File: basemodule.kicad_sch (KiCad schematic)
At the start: 6 parts, among them J1 Conn_01x05_Pin, J2 USB_C_Receptacle_USB2.0_14P, U1 ESP32-S3-WROOM-1, U2 LD1117S33TR_SOT223

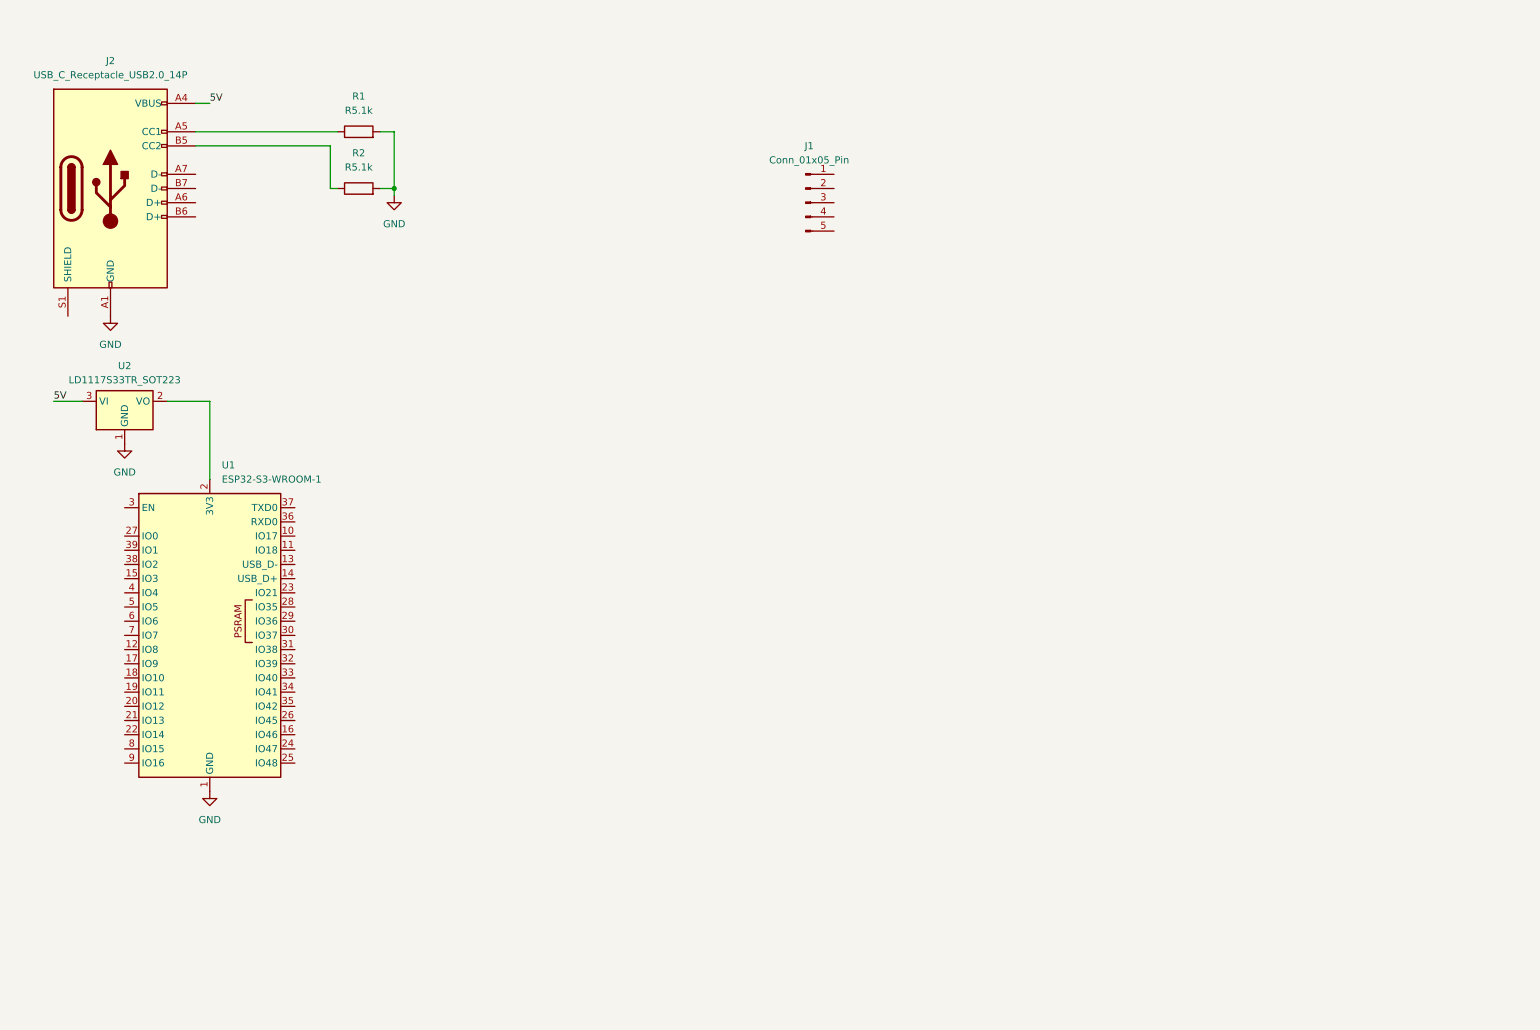
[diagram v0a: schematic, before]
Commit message: Added power components to base module schematic Higher-voltage (15V) USB PD is not complete, still need to read the datasheet for the PD chip. Also I just realized that PD chip is QFN, I have no idea how we are going to solder these onto the board. I hope we have access to a hot-air station or some other way of solder reflow.
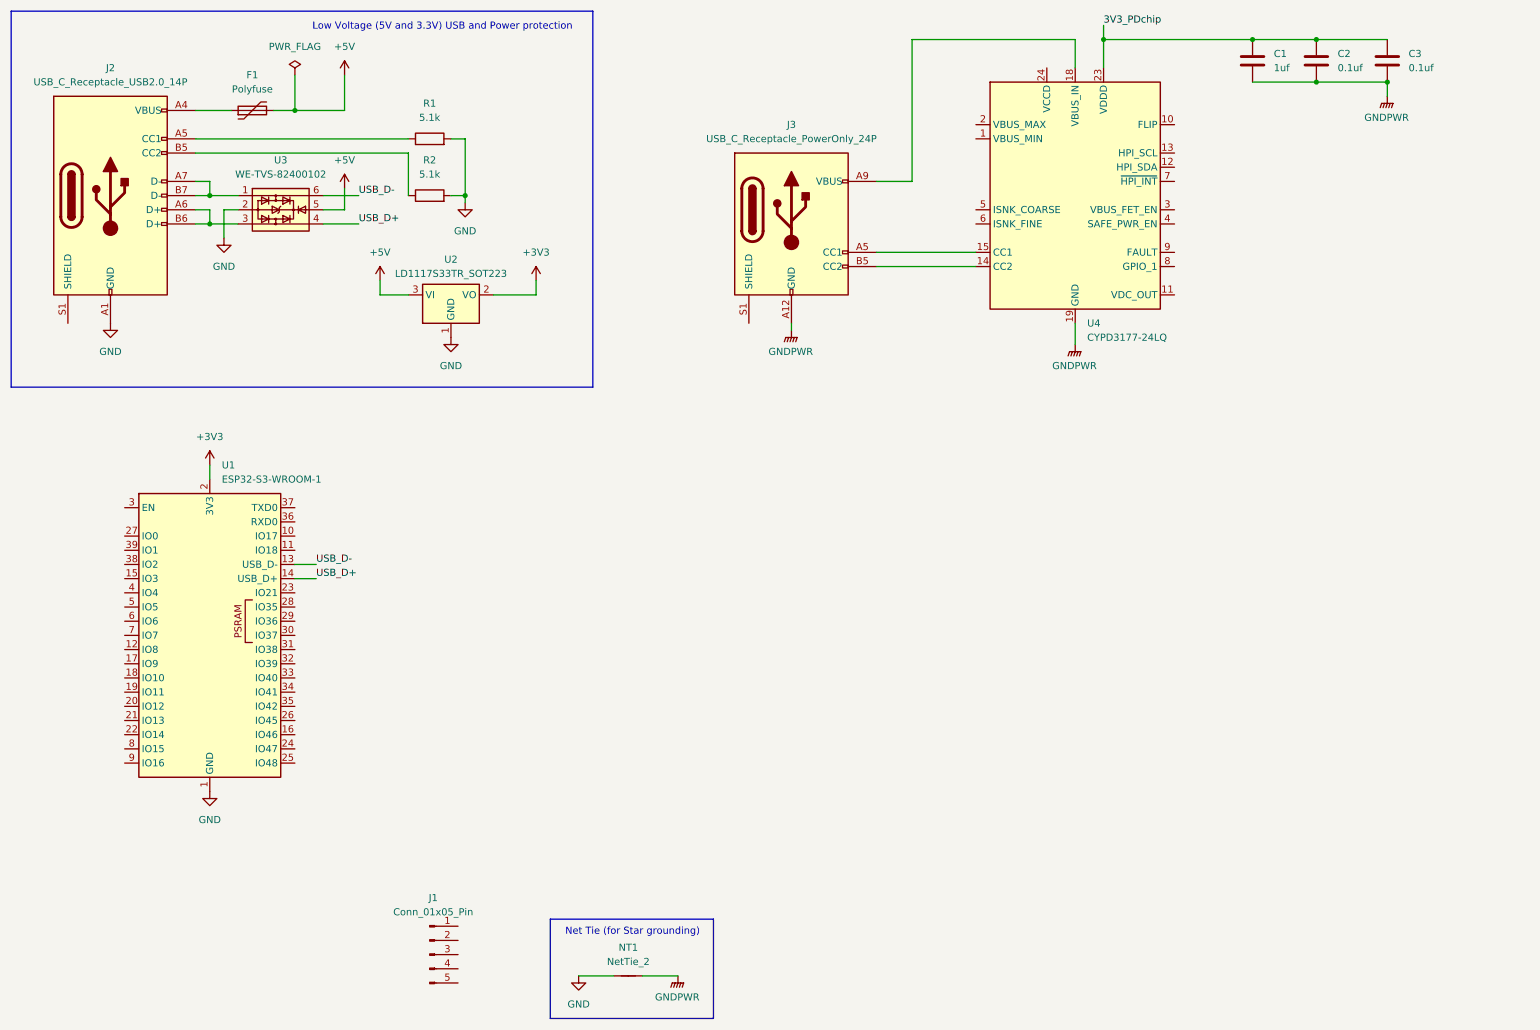
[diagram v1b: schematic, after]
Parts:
- added C1: 1uf, symbol Device:C
- added C2, C3: 0.1uf, symbol Device:C
- added F1: Polyfuse, Resistor_SMD:R_1206_3216Metric, symbol Device:Polyfuse
- added J3: USB_C_Receptacle_PowerOnly_24P, symbol Connector:USB_C_Receptacle_PowerOnly_24P
- added NT1: NetTie_2, symbol Device:NetTie_2
- added U3: WE-TVS-82400102, Package_TO_SOT_SMD:SOT-23-6, symbol Power_Protection:WE-TVS-82400102
- added U4: CYPD3177-24LQ, Package_DFN_QFN:QFN-24-1EP_4x4mm_P0.5mm_EP2.75x2.75mm, symbol Interface_USB:CYPD3177-24LQ
- R1, R2: value R5.1k -> 5.1k
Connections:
- net GND: now also NT1.1, U3.2
- net USB_D-: now reaches U1.13 (USB_D-)
- net USB_D-: now also U3.6
- net USB_D+: now reaches U1.14 (USB_D+)
- net USB_D+: now also U3.4
- net +3V3: now reaches U1.2 (3V3), U2.2 (VO)
- net at J2.A6 (D+): now also J2.B6 (D+), U3.3
- net at J2.A7 (D-): now also J2.B7 (D-), U3.1
- net 5V: no longer names the net of J2.A4 (VBUS), J2.A9 (VBUS), J2.B4 (VBUS), J2.B9 (VBUS)
- net 5V: now also F1.1; no longer U2.3 (VI)
- new net: J3.A4 (VBUS), J3.A9 (VBUS), J3.B4 (VBUS), J3.B9 (VBUS), U4.18 (VBUS_IN)
- new net: J3.A5 (CC1), U4.15 (CC1)
- new net: J3.B5 (CC2), U4.14 (CC2)
- new net +5V: F1.2, U2.3 (VI), U3.5
- new net 3V3_PDchip: C1.1, C2.1, C3.1, U4.23 (VDDD)
- new net GNDPWR: C1.2, C2.2, C3.2, J3.A1 (GND), J3.A12 (GND), J3.B1 (GND), J3.B12 (GND), NT1.2, U4.19 (GND), U4.22 (GND), U4.25 (GND)
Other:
- note added: "Low Voltage (5V and 3.3V) USB and Power protection"
- note added: "Net Tie (for Star grounding)"
- moved on the sheet: J1, J2, R1, R2, U2

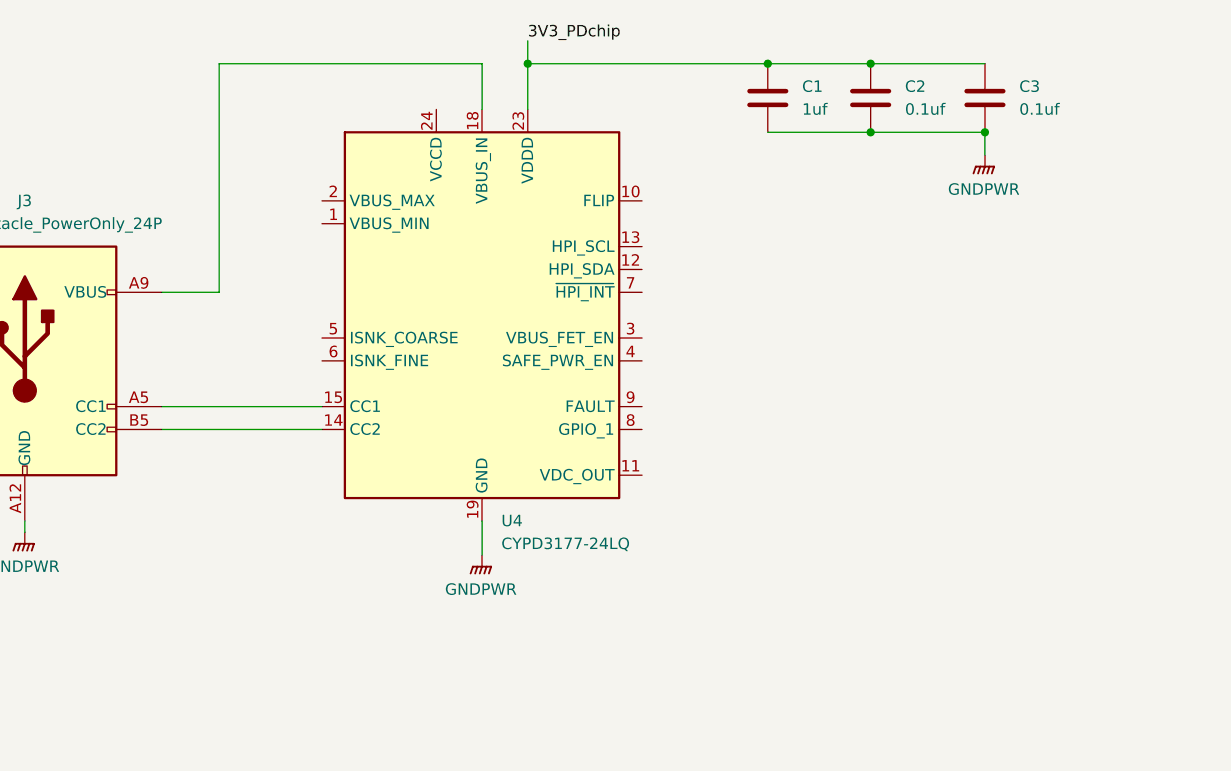
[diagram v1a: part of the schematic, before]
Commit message: Connect more components regarding PD 2SJ652 from ECE ESS seems like a good MOSFET
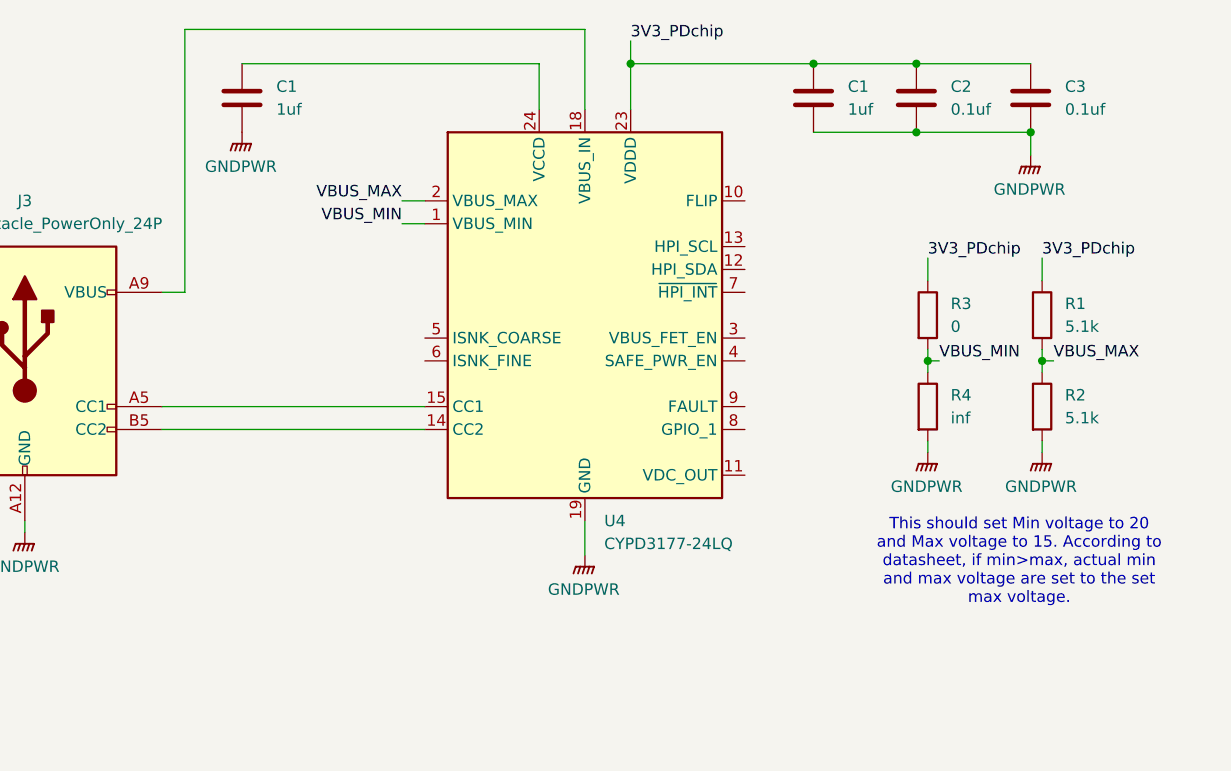
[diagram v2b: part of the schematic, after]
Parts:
- added C1: 1uf, symbol Device:C
- added R1, R2: 5.1k, symbol Device:R
- added R3: 0, symbol Device:R
- added R4: inf, symbol Device:R
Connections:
- net 3V3_PDchip: now also R1.1, R3.1
- net GNDPWR: now also C1.2, R2.2, R4.2
- net VBUS_MIN: now reaches U4.1 (VBUS_MIN)
- net VBUS_MIN: now also R3.2, R4.1
- net VBUS_MAX: now reaches U4.2 (VBUS_MAX)
- net VBUS_MAX: now also R1.2, R2.1
- net at U4.24 (VCCD): now also C1.1
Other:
- note added: "This should set Min voltage to 20 and Max voltage to 15. According to datasheet, if min>max, actual min and max voltage are set to the set max voltage."
- moved on the sheet: C1, C2, C3, U4
